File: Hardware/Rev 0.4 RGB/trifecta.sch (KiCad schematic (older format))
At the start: 263 parts, among them J1 USB2_C_Receptacle, SW1 SW_Push, SW2 Rotary_Encoder_Switch, SW3 Rotary_Encoder_Switch, SW4 Rotary_Encoder_Switch, U1 ATmega32U4-AU, U2 SRV05-4, Y1 16MHz

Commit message: Clean up silkscreens, Add ground fill, Generate new gerbers
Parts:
- R1, R6: value 10k -> 10kΩ
- R2, R3: value 5.1k -> 5.1kΩ
- R4, R5: value 22 -> 22Ω
- SW1: value SW_Push -> RESET
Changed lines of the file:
@@
 EESchema Schematic File Version 4
+LIBS:trifecta-cache
 EELAYER 30 0
 EELAYER END
@@
 P 3350 4100
 F 0 "R5" V 3154 4100 50  0000 C CNN
-F 1 "22" V 3245 4100 50  0000 C CNN
+F 1 "22Ω" V 3245 4100 50  0000 C CNN
 F 2 "Resistor_SMD:R_0805_2012Metric" H 3350 4100 50  0001 C CNN
 F 3 "https://datasheet.lcsc.com/szlcsc/Uniroyal-Elec-0805W8F2202T5E_C17560.pdf" H 3350 4100 50  0001 C CNN
@@
 P 3650 4000
 F 0 "R4" V 3454 4000 50  0000 C CNN
-F 1 "22" V 3545 4000 50  0000 C CNN
+F 1 "22Ω" V 3545 4000 50  0000 C CNN
 F 2 "Resistor_SMD:R_0805_2012Metric" H 3650 4000 50  0001 C CNN
 F 3 "https://datasheet.lcsc.com/szlcsc/Uniroyal-Elec-0805W8F2202T5E_C17560.pdf" H 3650 4000 50  0001 C CNN
@@
 P 4050 2700
 F 0 "R1" H 4109 2746 50  0000 L CNN
-F 1 "10k" H 4109 2655 50  0000 L CNN
+F 1 "10kΩ" H 4109 2655 50  0000 L CNN
 F 2 "Resistor_SMD:R_0805_2012Metric" H 4050 2700 50  0001 C CNN
 F 3 "https://datasheet.lcsc.com/szlcsc/Uniroyal-Elec-0805W8F1002T5E_C17414.pdf" H 4050 2700 50  0001 C CNN
@@
 P 6250 5100
 F 0 "R6" V 6054 5100 50  0000 C CNN
-F 1 "10k" V 6145 5100 50  0000 C CNN
+F 1 "10kΩ" V 6145 5100 50  0000 C CNN
 F 2 "Resistor_SMD:R_0805_2012Metric" H 6250 5100 50  0001 C CNN
 F 3 "https://datasheet.lcsc.com/szlcsc/Uniroyal-Elec-0805W8F1002T5E_C17414.pdf" H 6250 5100 50  0001 C CNN
@@
 P 7750 3250
 F 0 "R2" V 7554 3250 50  0000 C CNN
-F 1 "5.1k" V 7645 3250 50  0000 C CNN
+F 1 "5.1kΩ" V 7645 3250 50  0000 C CNN
 F 2 "Resistor_SMD:R_0805_2012Metric" H 7750 3250 50  0001 C CNN
 F 3 "https://datasheet.lcsc.com/szlcsc/Uniroyal-Elec-0805W8F5101T5E_C27834.pdf" H 7750 3250 50  0001 C CNN
@@
 P 8050 3350
 F 0 "R3" V 7854 3350 50  0000 C CNN
-F 1 "5.1k" V 7945 3350 50  0000 C CNN
+F 1 "5.1kΩ" V 7945 3350 50  0000 C CNN
 F 2 "Resistor_SMD:R_0805_2012Metric" H 8050 3350 50  0001 C CNN
 F 3 "https://datasheet.lcsc.com/szlcsc/Uniroyal-Elec-0805W8F5101T5E_C27834.pdf" H 8050 3350 50  0001 C CNN
@@
 P 3550 3000
 F 0 "SW1" H 3550 3285 50  0000 C CNN
-F 1 "SW_Push" H 3550 3194 50  0000 C CNN
+F 1 "RESET" H 3550 3194 50  0000 C CNN
 F 2 "random-keyboard-parts:SKQG-1155865" H 3550 3200 50  0001 C CNN
 F 3 "~" H 3550 3200 50  0001 C CNN

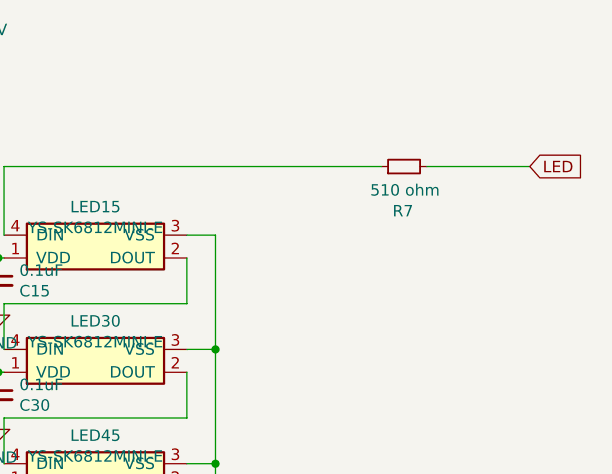
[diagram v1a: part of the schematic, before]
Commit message: Edit resistor silkscreen, Generate Gerbers
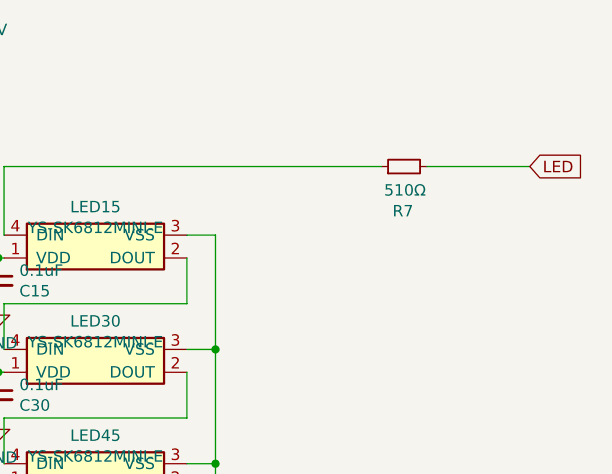
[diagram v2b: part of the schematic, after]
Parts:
- R7: value 510 ohm -> 510Ω
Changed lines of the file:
@@
 P 24325 2675
 F 0 "R7" V 24130 2680 50  0000 C CNN
-F 1 "510 ohm" V 24221 2671 50  0000 C CNN
+F 1 "510Ω" V 24221 2671 50  0000 C CNN
 F 2 "Resistor_SMD:R_0805_2012Metric" H 24325 2675 50  0001 C CNN
 F 3 "https://datasheet.lcsc.com/szlcsc/Uniroyal-Elec-0805W8F5100T5E_C17734.pdf" H 24325 2675 50  0001 C CNN
